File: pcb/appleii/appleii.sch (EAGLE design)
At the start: 17 parts, among them J1 POWER_JACKPTH, J2 ATX24RH

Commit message: working on appleii
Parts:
- removed JP3: (no value), atx_power_control:PINHD-1X4
- added C5: (no value), capacitor-wima:C5/2.5
- added JP4: (no value), appleii:4PIN_FAN
- JP1: device atx_power_control:PINHD-1X4 -> appleii:4PIN_FAN
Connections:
- net +12V: now also C1.+, JP1.2_VCC; no longer JP1.3
- net +5V: now also C2.+, JP4.2_VCC; no longer JP3.3
- net -5V: now also C5.1
- net GND: now also C1.-, C2.-, C3.2, C4.2, C5.2, JP1.1_GND, JP4.1_GND; no longer JP1.4, JP3.4
- net N$6: now also C4.1
- net N$8: now also C3.1
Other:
- moved on the sheet: C1, C2, C3, C4

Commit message: working on appleii
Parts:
- added U$7: VH396_2P, 396_conn:VH396_2P
- J1: device SparkFun:POWER_JACKPTH -> appleii:POWER_JACKPTH
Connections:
- new net N$1: J1.PWR, U$7.P$2
- net GND: now also J1.GND, J1.GNDBREAK, U$7.P$1
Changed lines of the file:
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@@
 <part name="P-4" library="supply1" library_urn="urn:adsk.eagle:library:371" deviceset="-5V" device=""/>
 <part name="P-5" library="supply1" library_urn="urn:adsk.eagle:library:371" deviceset="-5V" device=""/>
-<part name="J1" library="SparkFun" deviceset="POWER_JACK" device="PTH"/>
+<part name="J1" library="appleii" deviceset="POWER_JACK" device="PTH"/>
 <part name="C2" library="rcl" library_urn="urn:adsk.eagle:library:334" deviceset="CPOL-US" device="E5-10.5" package3d_urn="urn:adsk.eagle:package:23372/2"/>
 <part name="C1" library="rcl" library_urn="urn:adsk.eagle:library:334" deviceset="CPOL-US" device="E5-10.5" package3d_urn="urn:adsk.eagle:package:23372/2"/>
@@
 <part name="JP4" library="appleii" deviceset="4PIN_FAN" device=""/>
 <part name="JP1" library="appleii" deviceset="4PIN_FAN" device=""/>
+<part name="U$7" library="396_conn" deviceset="VH396_2P" device=""/>
+<part name="GND12" library="supply1" library_urn="urn:adsk.eagle:library:371" deviceset="GND" device=""/>
+<part name="GND13" library="supply1" library_urn="urn:adsk.eagle:library:371" deviceset="GND" device=""/>
 </parts>
 <sheets>
@@
 <instance part="JP4" gate="A" x="15.24" y="96.52" smashed="yes"/>
 <instance part="JP1" gate="A" x="15.24" y="127" smashed="yes"/>
+<instance part="U$7" gate="G$1" x="187.96" y="144.78" smashed="yes"/>
+<instance part="GND12" gate="1" x="203.2" y="142.24" smashed="yes">
+<attribute name="VALUE" x="200.66" y="139.7" size="1.778" layer="96"/>
+</instance>
+<instance part="GND13" gate="1" x="172.72" y="132.08" smashed="yes">
+<attribute name="VALUE" x="170.18" y="129.54" size="1.778" layer="96"/>
+</instance>
 </instances>
 <busses>
@@
 <wire x1="2.54" y1="134.62" x2="-15.24" y2="134.62" width="0.1524" layer="91"/>
 </segment>
+<segment>
+<pinref part="J1" gate="G$1" pin="GNDBREAK"/>
+<pinref part="J1" gate="G$1" pin="GND"/>
+<wire x1="167.64" y1="139.7" x2="167.64" y2="137.16" width="0.1524" layer="91"/>
+<pinref part="GND13" gate="1" pin="GND"/>
+<wire x1="167.64" y1="137.16" x2="172.72" y2="137.16" width="0.1524" layer="91"/>
+<wire x1="172.72" y1="137.16" x2="172.72" y2="134.62" width="0.1524" layer="91"/>
+<junction x="167.64" y="137.16"/>
+</segment>
+<segment>
+<pinref part="U$7" gate="G$1" pin="P$1"/>
+<pinref part="GND12" gate="1" pin="GND"/>
+<wire x1="182.88" y1="144.78" x2="203.2" y2="144.78" width="0.1524" layer="91"/>
+</segment>
 </net>
 <net name="-12V" class="0">
@@
 </segment>
 </net>
+<net name="N$1" class="0">
+<segment>
+<pinref part="J1" gate="G$1" pin="PWR"/>
+<pinref part="U$7" gate="G$1" pin="P$2"/>
+<wire x1="167.64" y1="142.24" x2="182.88" y2="142.24" width="0.1524" layer="91"/>
+</segment>
+</net>

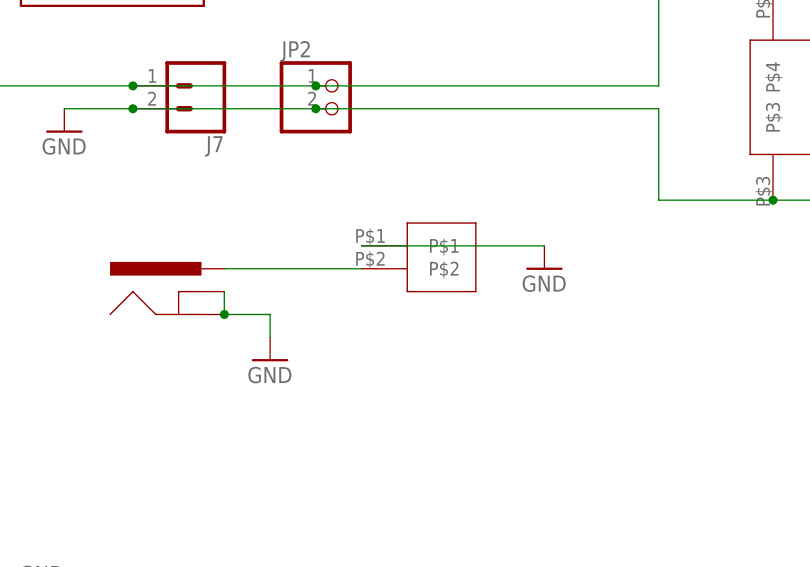
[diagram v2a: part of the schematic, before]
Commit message: updated silkscreen and switched to terminal block for power input
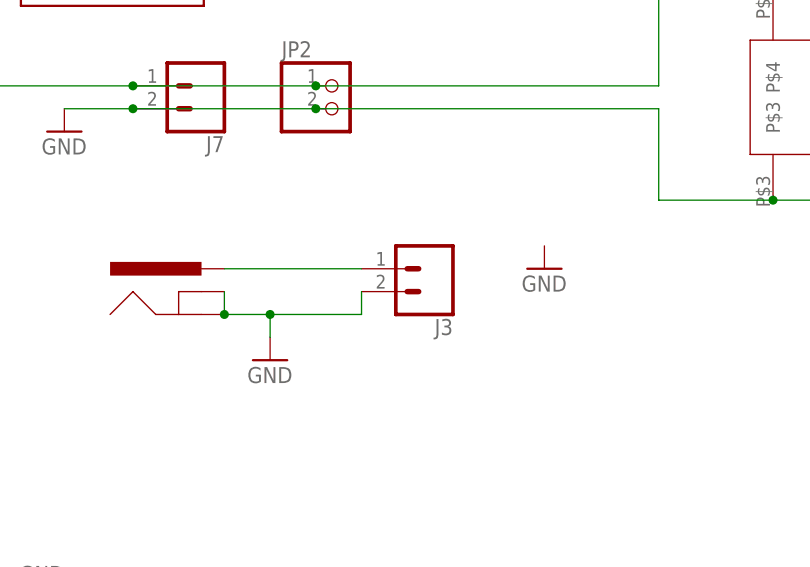
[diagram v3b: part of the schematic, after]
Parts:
- removed U$7: VH396_2P, 396_conn:VH396_2P
- added J3: (no value), atx_power_control:CONN_023.5MM-NO_SILK
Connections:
- net GND: now also J3.2; no longer U$7.P$1
- net N$1: now also J3.1; no longer U$7.P$2
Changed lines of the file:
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@@
 <part name="JP4" library="appleii" deviceset="4PIN_FAN" device=""/>
 <part name="JP1" library="appleii" deviceset="4PIN_FAN" device=""/>
-<part name="U$7" library="396_conn" deviceset="VH396_2P" device=""/>
 <part name="GND12" library="supply1" library_urn="urn:adsk.eagle:library:371" deviceset="GND" device=""/>
 <part name="GND13" library="supply1" library_urn="urn:adsk.eagle:library:371" deviceset="GND" device=""/>
+<part name="J3" library="atx_power_control" deviceset="CONN_02" device="3.5MM-NO_SILK"/>
 </parts>
 <sheets>
@@
 <instance part="JP4" gate="A" x="15.24" y="96.52" smashed="yes"/>
 <instance part="JP1" gate="A" x="15.24" y="127" smashed="yes"/>
-<instance part="U$7" gate="G$1" x="187.96" y="144.78" smashed="yes"/>
 <instance part="GND12" gate="1" x="203.2" y="142.24" smashed="yes">
 <attribute name="VALUE" x="200.66" y="139.7" size="1.778" layer="96"/>
@@
 <instance part="GND13" gate="1" x="172.72" y="132.08" smashed="yes">
 <attribute name="VALUE" x="170.18" y="129.54" size="1.778" layer="96"/>
+</instance>
+<instance part="J3" gate="G$1" x="190.5" y="142.24" smashed="yes" rot="R180">
+<attribute name="VALUE" x="193.04" y="147.066" size="1.778" layer="96" font="vector" rot="R180"/>
+<attribute name="NAME" x="193.04" y="136.652" size="1.778" layer="95" font="vector" rot="R180"/>
 </instance>
 </instances>
@@
 <wire x1="172.72" y1="137.16" x2="172.72" y2="134.62" width="0.1524" layer="91"/>
 <junction x="167.64" y="137.16"/>
-</segment>
-<segment>
-<pinref part="U$7" gate="G$1" pin="P$1"/>
-<pinref part="GND12" gate="1" pin="GND"/>
-<wire x1="182.88" y1="144.78" x2="203.2" y2="144.78" width="0.1524" layer="91"/>
+<pinref part="J3" gate="G$1" pin="2"/>
+<wire x1="182.88" y1="139.7" x2="182.88" y2="137.16" width="0.1524" layer="91"/>
+<wire x1="182.88" y1="137.16" x2="172.72" y2="137.16" width="0.1524" layer="91"/>
+<junction x="172.72" y="137.16"/>
 </segment>
 </net>
@@
 <segment>
 <pinref part="J1" gate="G$1" pin="PWR"/>
-<pinref part="U$7" gate="G$1" pin="P$2"/>
+<pinref part="J3" gate="G$1" pin="1"/>
 <wire x1="167.64" y1="142.24" x2="182.88" y2="142.24" width="0.1524" layer="91"/>
 </segment>
